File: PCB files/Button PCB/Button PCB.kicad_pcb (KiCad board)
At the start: 2 copper layers, 42.9 x 42.9 mm, 2 parts, among them SW1 TS-1102S-C-A-B, U1 X6511WVS-02H-C60D48R2

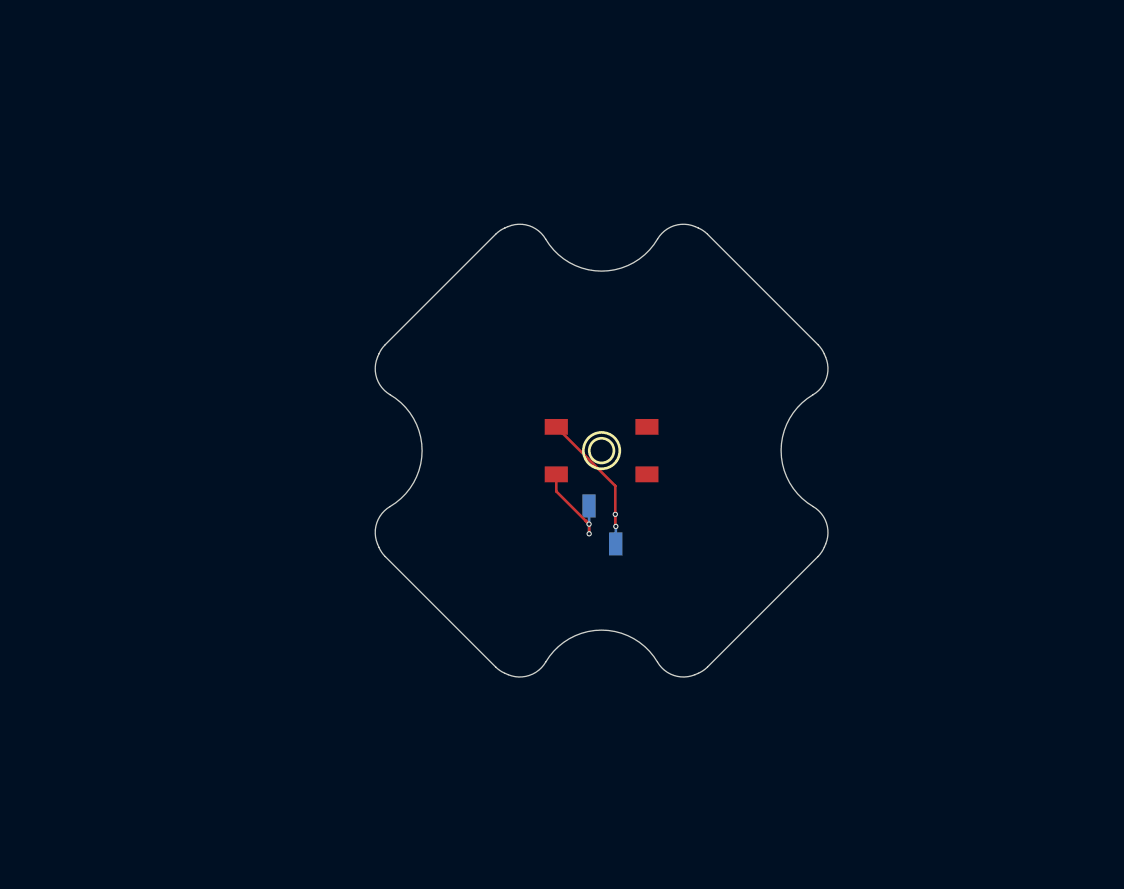
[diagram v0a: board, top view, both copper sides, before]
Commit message: started redesign of pcb and added test for atopile
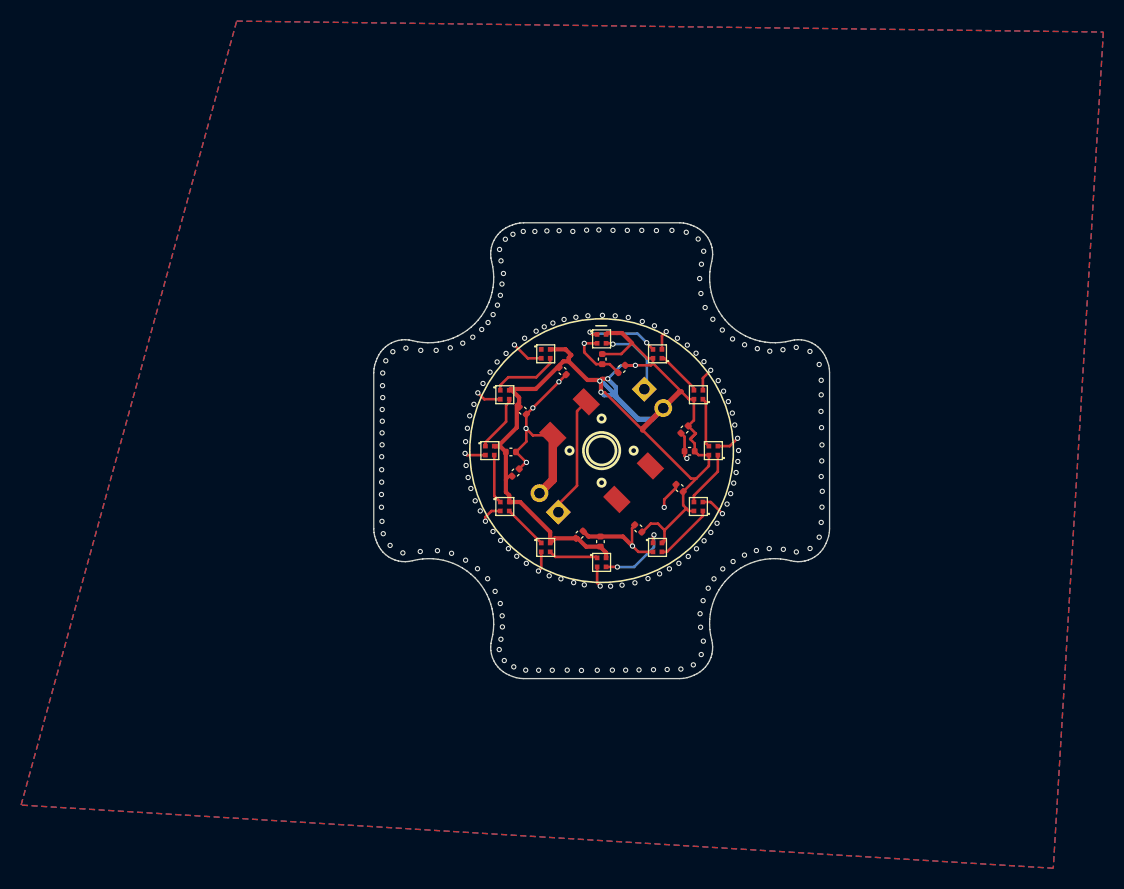
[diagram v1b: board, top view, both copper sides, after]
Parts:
- added C1: 0.1uF, Capacitor_SMD:C_0402_1005Metric, F.Cu at (131.8, 77.9)
- added C10: 0.1uF, Capacitor_SMD:C_0402_1005Metric, F.Cu at (123.1, 86.7)
- added C11: 0.1uF, Capacitor_SMD:C_0402_1005Metric, F.Cu at (124.3, 82.8)
- added C12: 0.1uF, Capacitor_SMD:C_0402_1005Metric, F.Cu at (128.0, 79.0)
- added C2: 0.1uF, Capacitor_SMD:C_0402_1005Metric, F.Cu at (133.6, 78.8)
- added C3: 0.1uF, Capacitor_SMD:C_0402_1005Metric, F.Cu at (139.6, 84.6)
- added C4: 0.1uF, Capacitor_SMD:C_0402_1005Metric, F.Cu at (140.1, 86.7)
- added C5: 0.1uF, Capacitor_SMD:C_0402_1005Metric, F.Cu at (139.1, 90.2)
- added C6: 0.1uF, Capacitor_SMD:C_0402_1005Metric, F.Cu at (135.2, 94.0)
- added C7: 0.1uF, Capacitor_SMD:C_0402_1005Metric, F.Cu at (131.6, 95.2)
- added C8: 0.1uF, Capacitor_SMD:C_0402_1005Metric, F.Cu at (129.7, 94.6)
- added C9: 0.1uF, Capacitor_SMD:C_0402_1005Metric, F.Cu at (123.6, 88.7)
- added LED1: XL-1010RGBC-WS2812B, footprint:LED-SMD_4P-L1.0-W1.0-TL_XL-1010RGBC-WS2812B, F.Cu at (131.7, 76.0)
- added LED10: XL-1010RGBC-WS2812B, footprint:LED-SMD_4P-L1.0-W1.0-TL_XL-1010RGBC-WS2812B, F.Cu at (121.1, 86.6)
- added LED11: XL-1010RGBC-WS2812B, footprint:LED-SMD_4P-L1.0-W1.0-TL_XL-1010RGBC-WS2812B, F.Cu at (122.6, 81.3)
- added LED12: XL-1010RGBC-WS2812B, footprint:LED-SMD_4P-L1.0-W1.0-TL_XL-1010RGBC-WS2812B, F.Cu at (126.4, 77.4)
- added LED2: XL-1010RGBC-WS2812B, footprint:LED-SMD_4P-L1.0-W1.0-TL_XL-1010RGBC-WS2812B, F.Cu at (137.0, 77.4)
- added LED3: XL-1010RGBC-WS2812B, footprint:LED-SMD_4P-L1.0-W1.0-TL_XL-1010RGBC-WS2812B, F.Cu at (140.9, 81.3)
- added LED4: XL-1010RGBC-WS2812B, footprint:LED-SMD_4P-L1.0-W1.0-TL_XL-1010RGBC-WS2812B, F.Cu at (142.3, 86.6)
- added LED5: XL-1010RGBC-WS2812B, footprint:LED-SMD_4P-L1.0-W1.0-TL_XL-1010RGBC-WS2812B, F.Cu at (140.9, 91.9)
- added LED6: XL-1010RGBC-WS2812B, footprint:LED-SMD_4P-L1.0-W1.0-TL_XL-1010RGBC-WS2812B, F.Cu at (137.0, 95.8)
- added LED7: XL-1010RGBC-WS2812B, footprint:LED-SMD_4P-L1.0-W1.0-TL_XL-1010RGBC-WS2812B, F.Cu at (131.7, 97.2)
- added LED8: XL-1010RGBC-WS2812B, footprint:LED-SMD_4P-L1.0-W1.0-TL_XL-1010RGBC-WS2812B, F.Cu at (126.4, 95.8)
- added LED9: XL-1010RGBC-WS2812B, footprint:LED-SMD_4P-L1.0-W1.0-TL_XL-1010RGBC-WS2812B, F.Cu at (122.6, 91.9)
- added U2: Conn_01x02_Pin, Connector_PinHeader_2.54mm:PinHeader_1x02_P2.54mm_Vertical, B.Cu at (135.8, 80.8)
- U1: value X6511WVS-02H-C60D48R2 -> Conn_01x02_Pin; footprint footprint:HDR-SMD_2P-P2.54_XKB_X6511WVS-02H-C60D48R2 -> Connector_PinHeader_2.54mm:PinHeader_1x02_P2.54mm_Vertical
- moved U1 4.35 mm to (127.6, 92.4), turned to 45 degrees
- turned SW1 to -45 degrees
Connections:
- U1 pad 1: GND -> BUTTON
- U1 pad 2: BUTTON -> GND
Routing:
- net +5V: track 0.00 -> 114.7 mm, vias 0 -> 4
- net GND: track 10.0 -> 63.7 mm, vias 2 -> 196
- net LED DATA: track 0.00 -> 7.46 mm, vias 0 -> 1
- net Net-(LED1-DOUT): track 0.00 -> 7.43 mm, vias 0 -> 2
- net Net-(LED6-DOUT): track 0.00 -> 7.30 mm, vias 0 -> 2
- net Net-(LED11-DOUT): track 0.00 -> 6.54 mm
- net Net-(LED5-DOUT): track 0.00 -> 5.77 mm
- net Net-(LED10-DOUT): track 0.00 -> 5.39 mm
- net Net-(LED4-DOUT): track 0.00 -> 5.39 mm
- net Net-(LED3-DOUT): track 0.00 -> 4.82 mm
- net Net-(LED10-DIN): track 0.00 -> 4.69 mm
- net Net-(LED7-DOUT): track 0.00 -> 4.69 mm
- net Net-(LED2-DOUT): track 0.00 -> 4.49 mm
- net Net-(LED8-DOUT): track 0.00 -> 4.29 mm
- net BUTTON: track 14.6 -> 11.6 mm, vias 2 -> 0
- added copper zone on B.Cu, net GND
- added copper zone on F.Cu, net GND
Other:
- board size 42.9 x 42.9 mm -> 43.2 x 43.2 mm
- board text added: "GlowLight/GlowTower Button PCB v2.0"
- board text added: "V D"
- board text removed: "GlowLight/GlowTower Button PCB"
